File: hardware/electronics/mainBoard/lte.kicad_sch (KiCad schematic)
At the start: 44 parts, among them J7 Bus_M.2_Socket_E, J8 M.2 Standoff, J9 M.2 Standoff, SW5 JS102011JCQN, SW6 JS102011JCQN, U11 TPS22996H-Q1, U12 TXS0108EQWRKSRQ1, U13 TXS0104VxRUTR

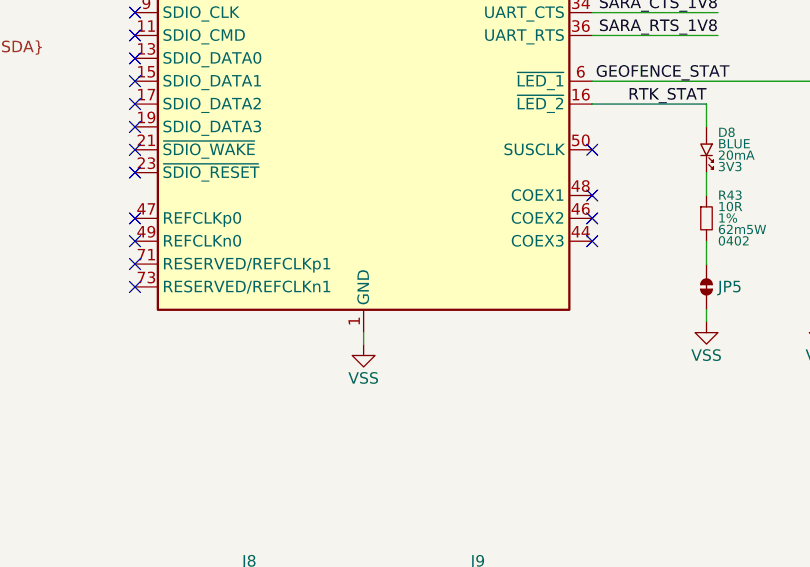
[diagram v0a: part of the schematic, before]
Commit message: added footprints to symbols
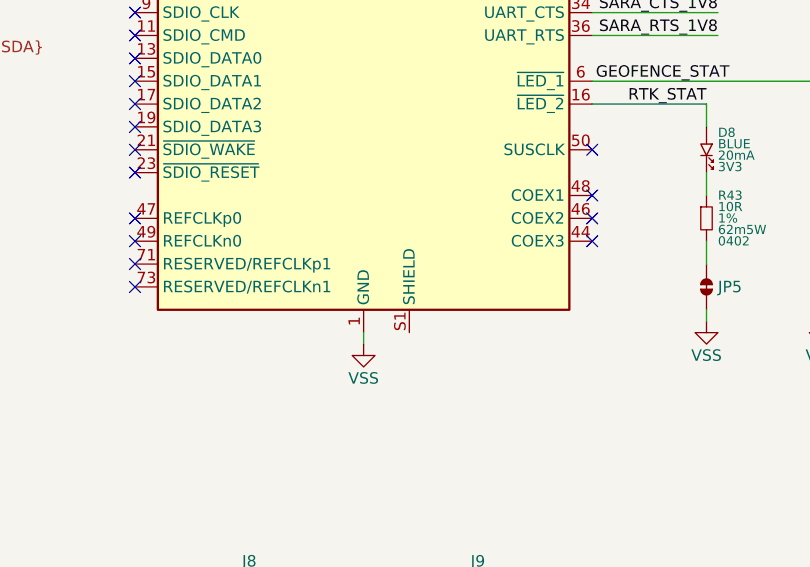
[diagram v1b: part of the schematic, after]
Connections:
- new net: J7.S1 (SHIELD), J7.S2 (SHIELD)
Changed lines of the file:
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@@
 		(pin "53"
+		)
+		(pin "S1"
+		)
+		(pin "S2"
 		)
 		(instances

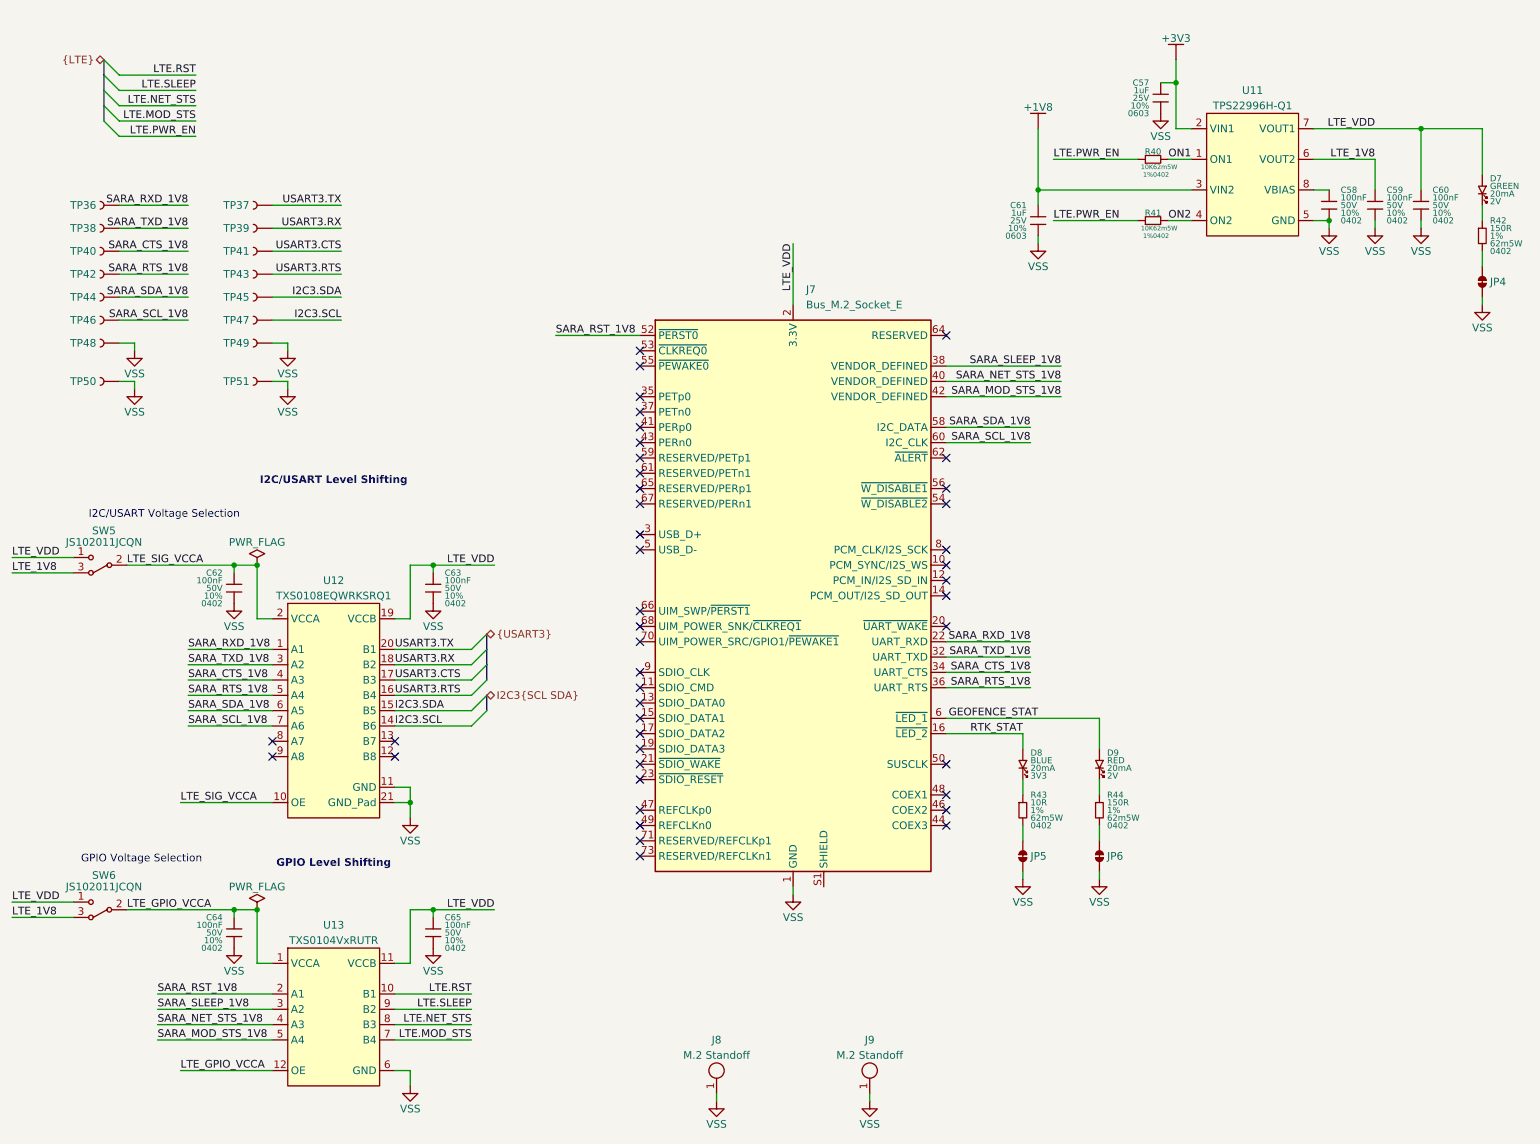
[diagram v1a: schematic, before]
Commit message: assigned footprints
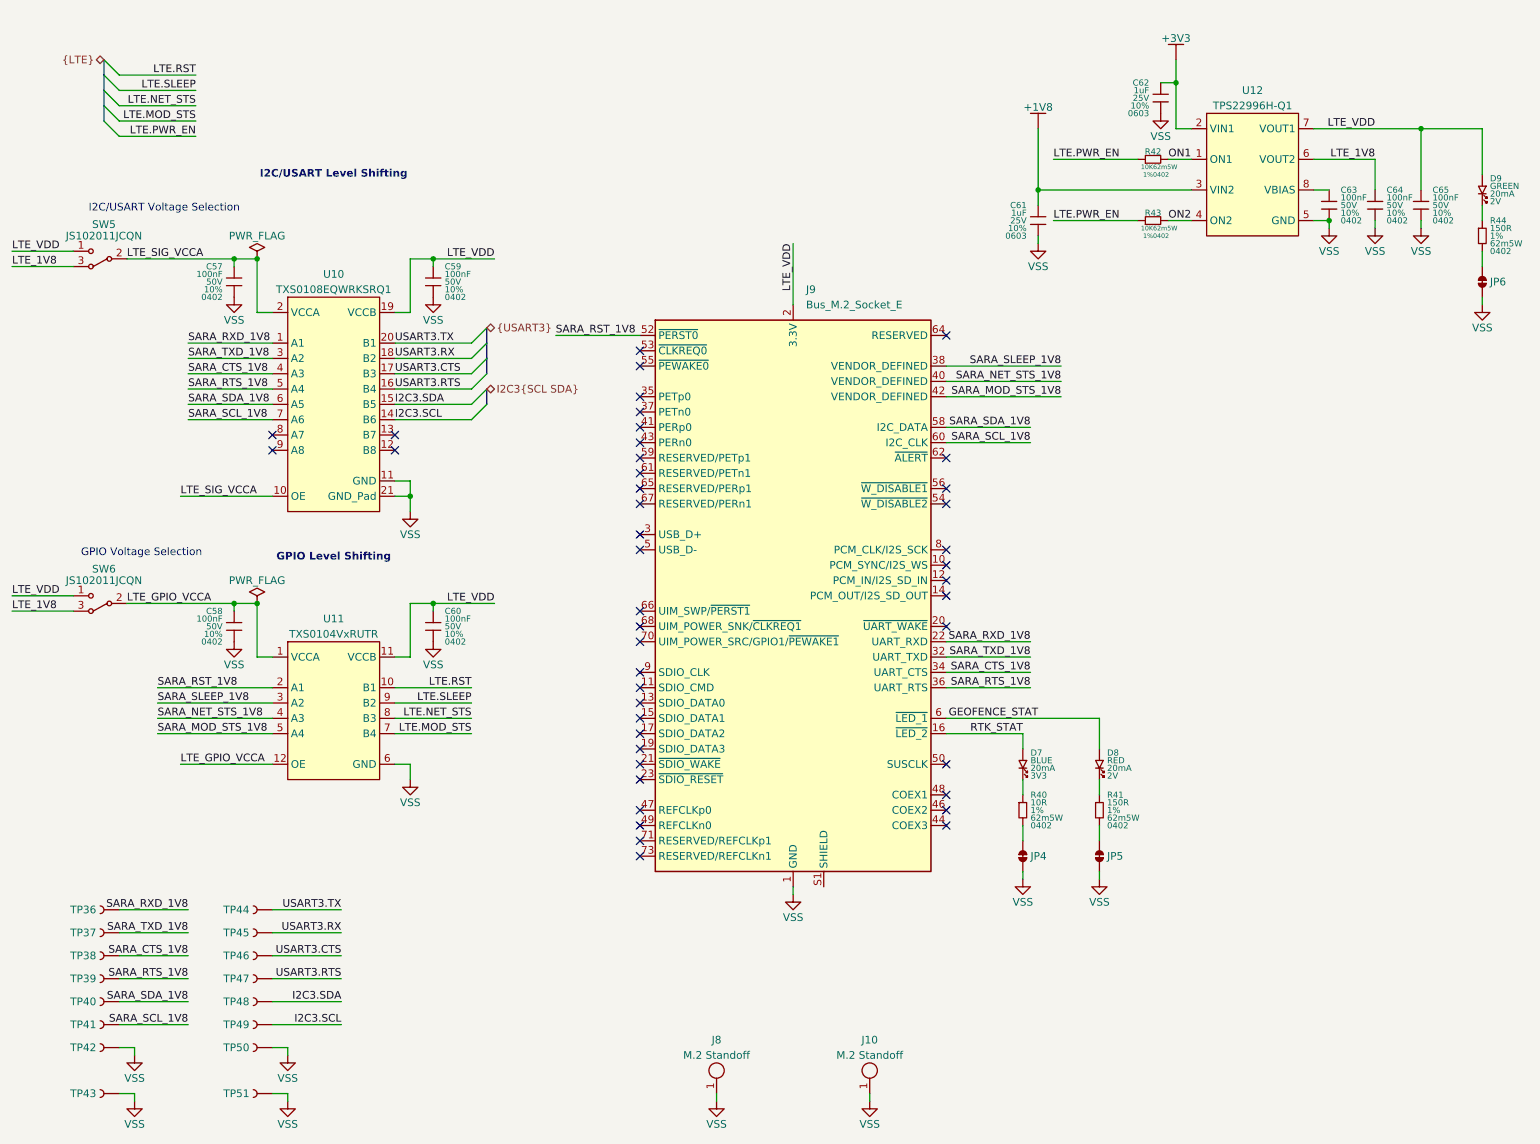
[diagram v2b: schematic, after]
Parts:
- C57: renamed from C62; footprint (none) -> lib_passives:GCM0402
- C58: renamed from C64; footprint (none) -> lib_passives:GCM0402
- C59: renamed from C63; footprint (none) -> lib_passives:GCM0402
- C60: renamed from C65; footprint (none) -> lib_passives:GCM0402
- C61: footprint (none) -> lib_passives:GRT0603
- C62: renamed from C57; footprint (none) -> lib_passives:GRT0603
- C63: renamed from C58; footprint (none) -> lib_passives:GCM0402
- C64: renamed from C59; footprint (none) -> lib_passives:GCM0402
- C65: renamed from C60; footprint (none) -> lib_passives:GCM0402
- D7: renamed from D8; footprint (none) -> lib_diodes:LTST-0603
- D8: renamed from D9; footprint (none) -> lib_diodes:LTST-0603
- D9: renamed from D7; footprint (none) -> lib_diodes:LTST-0603
- J10: renamed from J9; footprint (none) -> lib_misc:MountingHole_3.5mm_Pad_Via
- J8: footprint (none) -> lib_misc:MountingHole_3.5mm_Pad_Via
- JP4: renamed from JP5; footprint (none) -> lib_misc:SolderJumper-2_P1.3mm_Bridged_RoundedPad1.0x1.5mm
- JP5: renamed from JP6; footprint (none) -> lib_misc:SolderJumper-2_P1.3mm_Bridged_RoundedPad1.0x1.5mm
- JP6: renamed from JP4; footprint (none) -> lib_misc:SolderJumper-2_P1.3mm_Bridged_RoundedPad1.0x1.5mm
- R40: renamed from R43; footprint (none) -> lib_passives:CRCW0402
- R41: renamed from R44; footprint (none) -> lib_passives:CRCW0402
- R42: renamed from R40; footprint (none) -> lib_passives:CRCW0402
- R43: renamed from R41; footprint (none) -> lib_passives:CRCW0402
- R44: renamed from R42; footprint (none) -> lib_passives:CRCW0402
- TP36: footprint (none) -> lib_misc:TP_2mm
- TP37: renamed from TP38; footprint (none) -> lib_misc:TP_2mm
- TP38: renamed from TP40; footprint (none) -> lib_misc:TP_2mm
- TP39: renamed from TP42; footprint (none) -> lib_misc:TP_2mm
- TP40: renamed from TP44; footprint (none) -> lib_misc:TP_2mm
- TP41: renamed from TP46; footprint (none) -> lib_misc:TP_2mm
- TP42: renamed from TP48; footprint (none) -> lib_misc:TP_RCW
- TP43: renamed from TP50; footprint (none) -> lib_misc:TP_RCW
- TP44: renamed from TP37; footprint (none) -> lib_misc:TP_2mm
- TP45: renamed from TP39; footprint (none) -> lib_misc:TP_2mm
- TP46: renamed from TP41; footprint (none) -> lib_misc:TP_2mm
- TP47: renamed from TP43; footprint (none) -> lib_misc:TP_2mm
- TP48: renamed from TP45; footprint (none) -> lib_misc:TP_2mm
- TP49: renamed from TP47; footprint (none) -> lib_misc:TP_2mm
- TP50: renamed from TP49; footprint (none) -> lib_misc:TP_RCW
- TP51: footprint (none) -> lib_misc:TP_RCW
- U10: renamed from U12; footprint (none) -> lib_ICs:QFN50P450X250X100-20
- renumbered J7 to J9, U13 to U11, U11 to U12
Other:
- moved on the sheet: C57, C58, C59, C60, SW5, SW6, TP36, TP37, TP38, TP39, TP40, TP41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

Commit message: added UART RX/TX fixer pads for 0R resistors
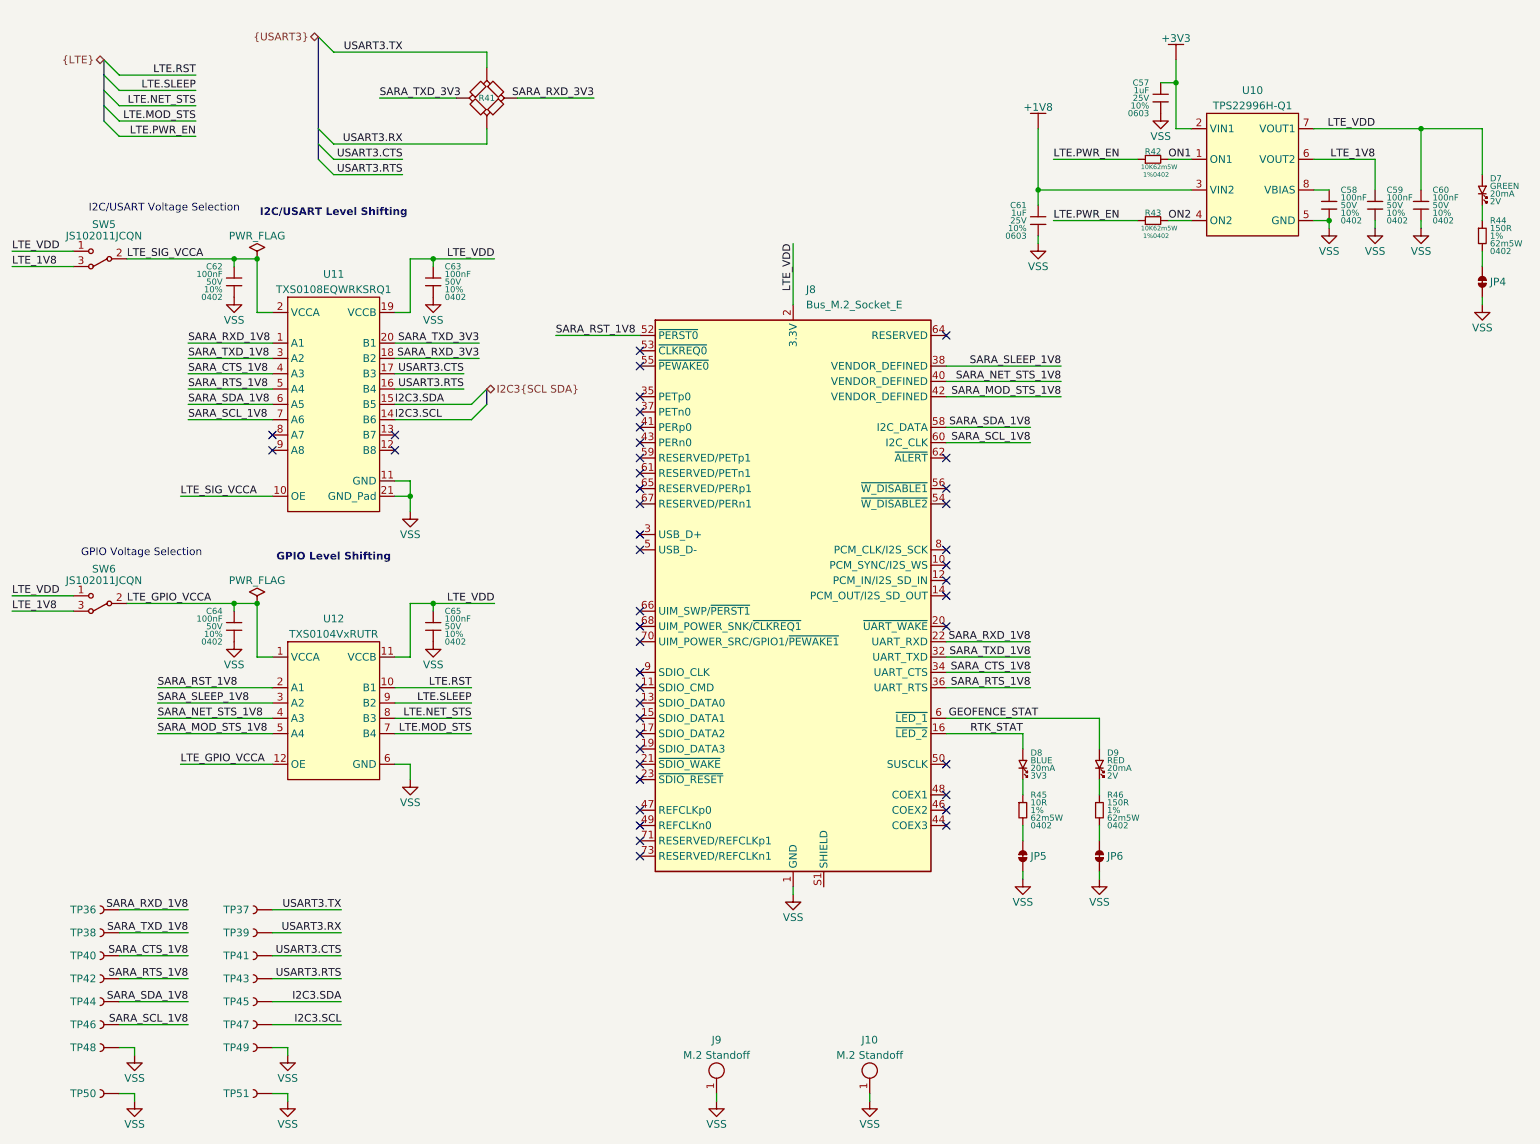
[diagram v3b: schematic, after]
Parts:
- added R41: ~, lib_passives:CRCW0402_QUAD_UART, symbol lib_sch:R_double
- renumbered C62 to C57, C63 to C58, C64 to C59, C65 to C60, C57 to C62, C59 to C63, C58 to C64, C60 to C65, D9 to D7, D7 to D8, D8 to D9, J9 to J8, J8 to J9, JP6 to JP4, JP4 to JP5, JP5 to JP6, R40 to R45, R41 to R46, TP44 to TP37, TP37 to TP38, TP45 to TP39, TP38 to TP40, TP46 to TP41, TP39 to TP42, TP47 to TP43, TP40 to TP44, TP48 to TP45, TP41 to TP46, TP49 to TP47, TP42 to TP48, TP50 to TP49, TP43 to TP50, U12 to U10, U10 to U11, U11 to U12
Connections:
- net USART3.RX: now also R41.3; no longer U11.18 (B2)
- net USART3.TX: now also R41.1; no longer U11.20 (B1)
- new net SARA_RXD_3V3: R41.2, U11.18 (B2)
- new net SARA_TXD_3V3: R41.4, U11.20 (B1)

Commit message: fixed sch
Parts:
- removed D8: LTST-C191TBKT, lib_diodes:LTST-0603, symbol lib_sch:LED
- removed D9: LTST-C191KRKT, lib_diodes:LTST-0603, symbol lib_sch:LED
- removed JP5, JP6: ~, lib_misc:SolderJumper-2_P1.3mm_Bridged_RoundedPad1.0x1.5mm, symbol lib_sch:Jumper_2_Bridged
- removed R45: 10R, lib_passives:CRCW0402, symbol lib_sch:R
- removed R46: 150R, lib_passives:CRCW0402, symbol lib_sch:R
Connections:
- net GEOFENCE_STAT: no longer names the net of J8.6 (~{LED_1})
- net RTK_STAT: no longer names the net of J8.16 (~{LED_2})
- no-connect marks 44 -> 46

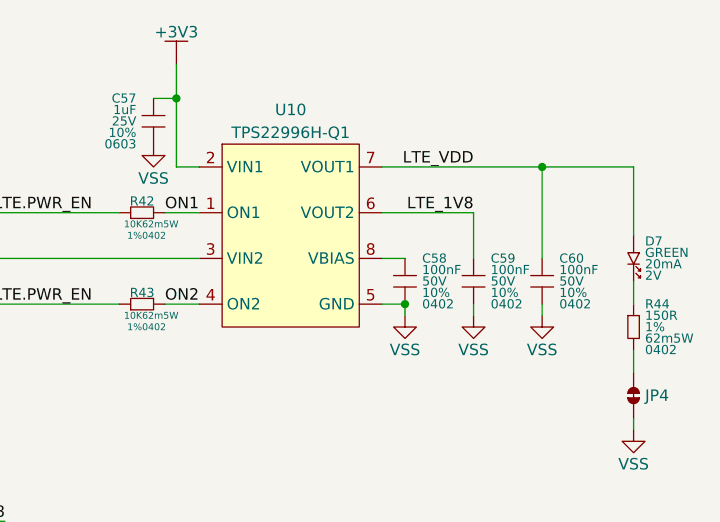
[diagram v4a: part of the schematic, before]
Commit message: fixed VBIAS net
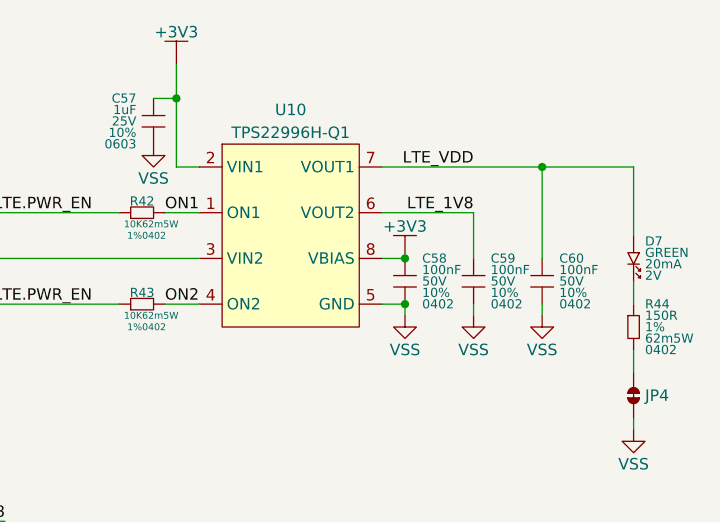
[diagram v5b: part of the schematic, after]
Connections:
- net +3V3: now also C58.1, U10.8 (VBIAS)
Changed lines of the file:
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@@
 	(title_block
 		(title "LTE Card")
-		(date "2025-03-20")
+		(date "2025-03-31")
 		(rev "1")
 		(comment 2 "PROTOTYPE")
@@
 	)
 	(junction
+		(at 228.6 40.64)
+		(diameter 0)
+		(color 0 0 0 0)
+	)
+	(junction
 		(at 50.8 52.07)
 		(diameter 0)
@@
 					(unit 1)
 				)
+			)
+		)
+	)
+	(symbol
+		(lib_id "lib_pwr:+3V3")
+		(at 228.6 40.64 0)
+		(unit 1)
+		(exclude_from_sim no)
+		(in_bom yes)
+		(on_board yes)
+		(dnp no)
+		(fields_autoplaced yes)
+		(property "Reference" "#PWR0120"
+			(at 228.6 40.64 0)
+			(effects
+				(font
+					(size 1.27 1.27)
+				)
+				(hide yes)
+			)
+		)
+		(property "Value" "+3V3"
+			(at 228.6 37.084 0)
+			(do_not_autoplace yes)
+			(effects
+				(font
+					(size 1.27 1.27)
+				)
+			)
+		)
+		(property "Footprint" ""
+			(at 228.6 40.64 0)
+			(effects
+				(font
+					(size 1.27 1.27)
+				)
+				(hide yes)
+			)
+		)
+		(property "Datasheet" ""
+			(at 228.6 40.64 0)
+			(effects
+				(font
+					(size 1.27 1.27)
+				)
+				(hide yes)
+			)
+		)
+		(property "Description" ""
+			(at 228.6 40.64 0)
+			(effects
+				(font
+					(size 1.27 1.27)
+				)
+				(hide yes)
+			)
+		)
+		(pin "1"
+		)
+		(instances
+			(project "mainBoard"
+				(path "/be16e32f-2ccf-4272-9ec7-94d5fe7a55e0/7ff6c767-11c2-4c6d-a16f-82c26617ef6d"
+					(reference "#PWR0120")
+					(unit 1)
+				)
